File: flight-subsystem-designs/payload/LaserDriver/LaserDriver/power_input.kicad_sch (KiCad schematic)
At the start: 13 parts, among them J1 VIN Pin Header, J6 VIN Banana, J7 GND Banana, U1 LDL212PV33R, U6 UCC33420RAQR

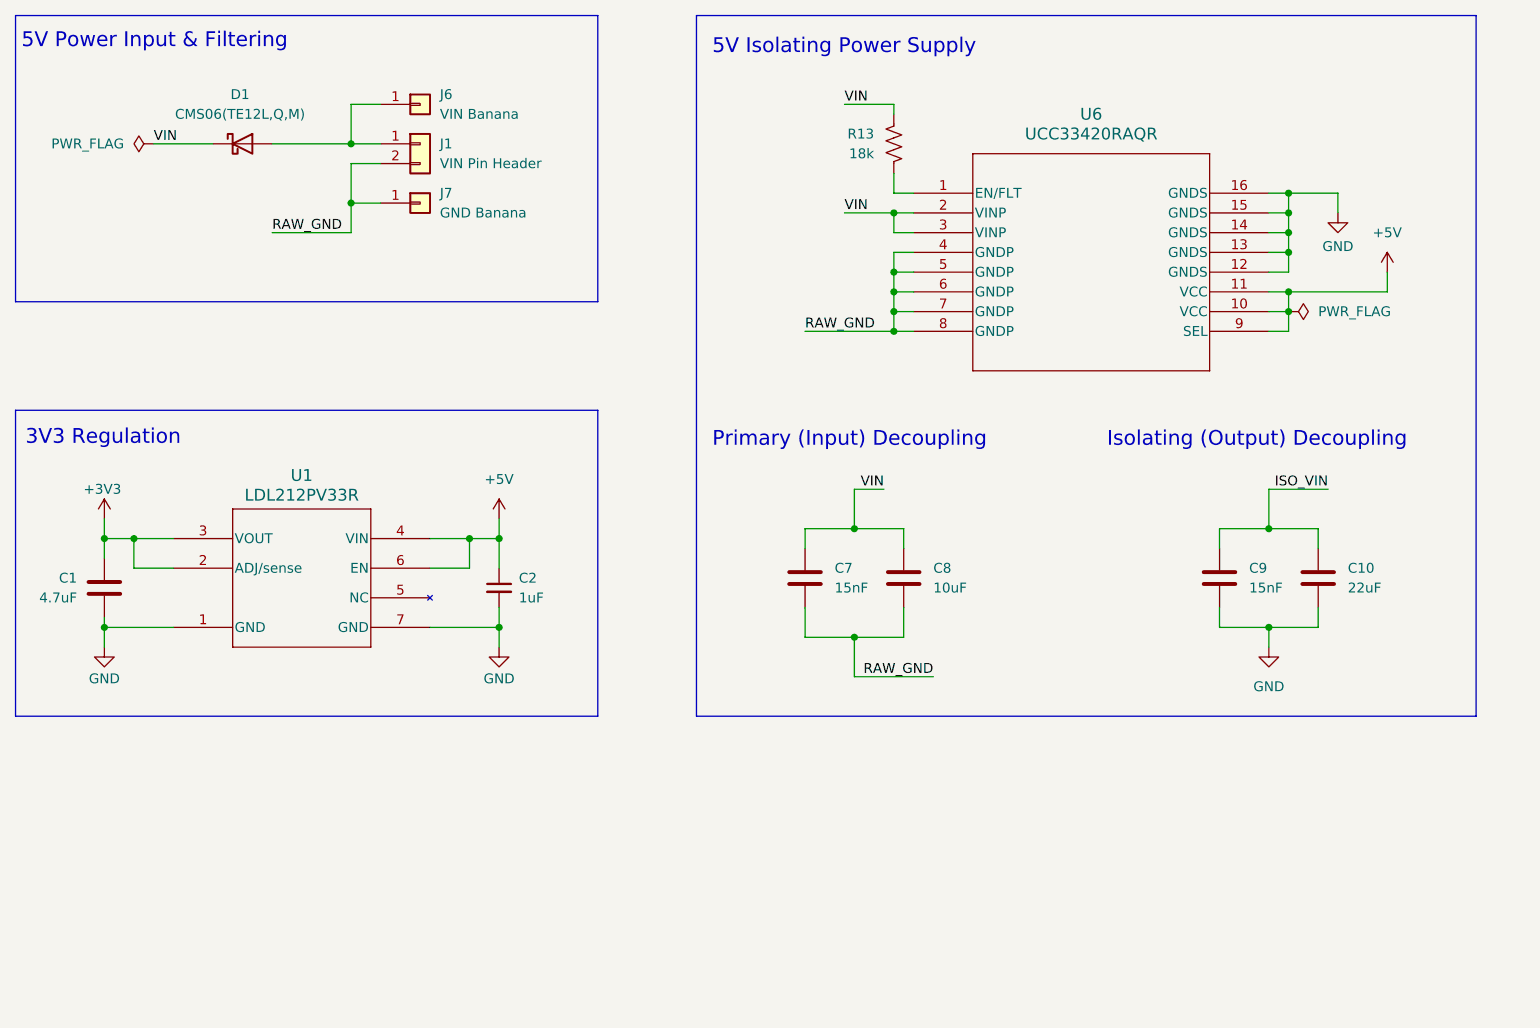
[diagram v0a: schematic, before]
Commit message: laserdriver: reset all annotations and cleared pcb :sob:
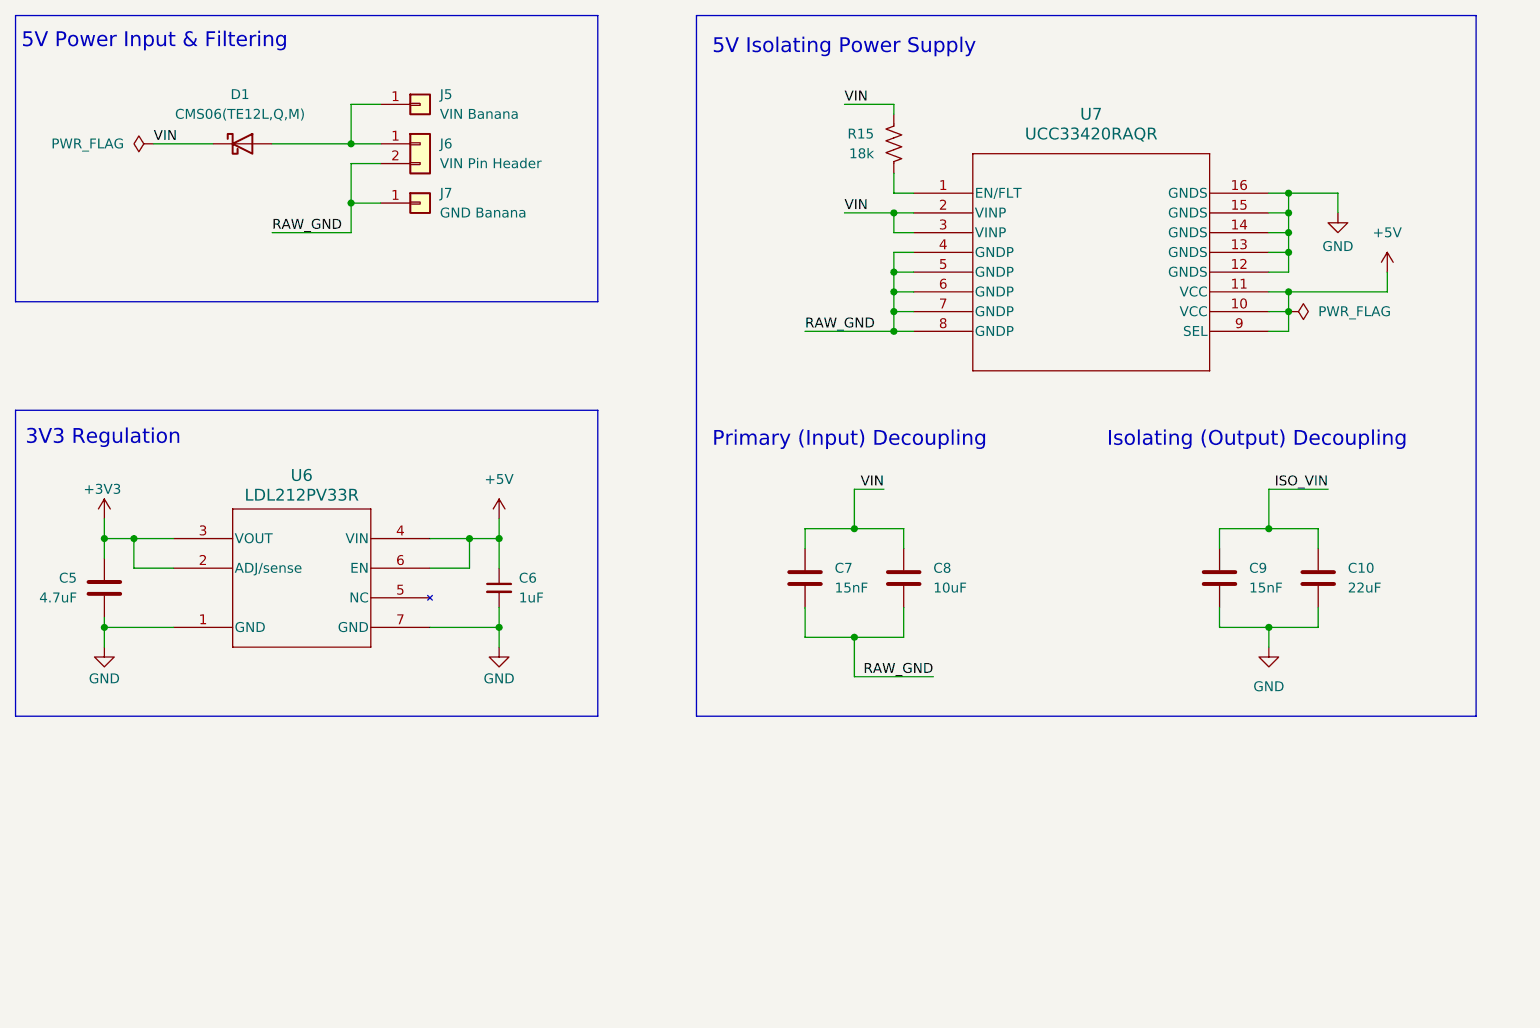
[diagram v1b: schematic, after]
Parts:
- renumbered C1 to C5, C2 to C6, J6 to J5, J1 to J6, R13 to R15, U1 to U6, U6 to U7
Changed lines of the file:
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@@
 		(on_board yes)
 		(dnp no)
-		(property "Reference" "#PWR02"
+		(property "Reference" "#PWR027"
 			(at 34.29 90.17 0)
 			(effects
@@
 			(project "LaserDriver"
 				(path "/f859ecae-83c7-438c-b2af-b7873d5255a0/55c34013-2f41-4006-a024-9ccd7006f77a"
-					(reference "#PWR02")
+					(reference "#PWR027")
 					(unit 1)
 				)
@@
 		(on_board yes)
 		(dnp no)
-		(property "Reference" "#PWR028"
+		(property "Reference" "#PWR032"
 			(at 193.04 53.34 0)
 			(effects
@@
 			(project ""
 				(path "/f859ecae-83c7-438c-b2af-b7873d5255a0/55c34013-2f41-4006-a024-9ccd7006f77a"
-					(reference "#PWR028")
+					(reference "#PWR032")
 					(unit 1)
 				)
@@
 		(dnp no)
 		(fields_autoplaced yes)
-		(property "Reference" "#PWR08"
+		(property "Reference" "#PWR031"
 			(at 184.15 109.22 0)
 			(effects
@@
 			(project ""
 				(path "/f859ecae-83c7-438c-b2af-b7873d5255a0/55c34013-2f41-4006-a024-9ccd7006f77a"
-					(reference "#PWR08")
+					(reference "#PWR031")
 					(unit 1)
 				)
@@
 		(dnp no)
 		(fields_autoplaced yes)
-		(property "Reference" "J1"
+		(property "Reference" "J6"
 			(at 77.47 38.0999 0)
 			(effects
@@
 			(project "LaserDriver"
 				(path "/f859ecae-83c7-438c-b2af-b7873d5255a0/55c34013-2f41-4006-a024-9ccd7006f77a"
-					(reference "J1")
+					(reference "J6")
 					(unit 1)
 				)
@@
 		(dnp no)
 		(fields_autoplaced yes)
-		(property "Reference" "J6"
+		(property "Reference" "J5"
 			(at 77.47 31.7499 0)
 			(effects
@@
 			(project ""
 				(path "/f859ecae-83c7-438c-b2af-b7873d5255a0/55c34013-2f41-4006-a024-9ccd7006f77a"
-					(reference "J6")
+					(reference "J5")
 					(unit 1)
 				)
@@
 		(on_board yes)
 		(dnp no)
-		(property "Reference" "C1"
+		(property "Reference" "C5"
 			(at 28.448 93.98 0)
 			(effects
@@
 			(project "LaserDriver"
 				(path "/f859ecae-83c7-438c-b2af-b7873d5255a0/55c34013-2f41-4006-a024-9ccd7006f77a"
-					(reference "C1")
+					(reference "C5")
 					(unit 1)
 				)
@@
 		(on_board yes)
 		(dnp no)
-		(property "Reference" "R13"
+		(property "Reference" "R15"
 			(at 133.35 36.8299 0)
 			(effects
@@
 			(project ""
 				(path "/f859ecae-83c7-438c-b2af-b7873d5255a0/55c34013-2f41-4006-a024-9ccd7006f77a"
-					(reference "R13")
+					(reference "R15")
 					(unit 1)
 				)
@@
 		(on_board yes)
 		(dnp no)
-		(property "Reference" "#PWR09"
+		(property "Reference" "#PWR030"
 			(at 85.09 109.22 0)
 			(effects
@@
 			(project "LaserDriver"
 				(path "/f859ecae-83c7-438c-b2af-b7873d5255a0/55c34013-2f41-4006-a024-9ccd7006f77a"
-					(reference "#PWR09")
+					(reference "#PWR030")
 					(unit 1)
 				)
@@
 		(on_board yes)
 		(dnp no)
-		(property "Reference" "#PWR03"
+		(property "Reference" "#PWR028"
 			(at 34.29 109.22 0)
 			(effects
@@
 			(project "LaserDriver"
 				(path "/f859ecae-83c7-438c-b2af-b7873d5255a0/55c34013-2f41-4006-a024-9ccd7006f77a"
-					(reference "#PWR03")
+					(reference "#PWR028")
 					(unit 1)
 				)
@@
 		(dnp no)
 		(fields_autoplaced yes)
-		(property "Reference" "#PWR033"
+		(property "Reference" "#PWR029"
 			(at 85.09 90.17 0)
 			(effects
@@
 			(project ""
 				(path "/f859ecae-83c7-438c-b2af-b7873d5255a0/55c34013-2f41-4006-a024-9ccd7006f77a"
-					(reference "#PWR033")
+					(reference "#PWR029")
 					(unit 1)
 				)
@@
 		(dnp no)
 		(fields_autoplaced yes)
-		(property "Reference" "C2"
+		(property "Reference" "C6"
 			(at 87.63 93.9862 0)
 			(effects
@@
 			(project "LaserDriver"
 				(path "/f859ecae-83c7-438c-b2af-b7873d5255a0/55c34013-2f41-4006-a024-9ccd7006f77a"
-					(reference "C2")
+					(reference "C6")
 					(unit 1)
 				)
@@
 		(dnp no)
 		(fields_autoplaced yes)
-		(property "Reference" "U6"
+		(property "Reference" "U7"
 			(at 161.29 34.29 0)
 			(effects
@@
 			(project ""
 				(path "/f859ecae-83c7-438c-b2af-b7873d5255a0/55c34013-2f41-4006-a024-9ccd7006f77a"
-					(reference "U6")
+					(reference "U7")
 					(unit 1)
 				)
@@
 		(on_board yes)
 		(dnp no)
-		(property "Reference" "U1"
+		(property "Reference" "U6"
 			(at 59.69 80.772 0)
 			(effects
@@
 			(project "LaserDriver"
 				(path "/f859ecae-83c7-438c-b2af-b7873d5255a0/55c34013-2f41-4006-a024-9ccd7006f77a"
-					(reference "U1")
+					(reference "U6")
 					(unit 1)
 				)
@@
 		(dnp no)
 		(fields_autoplaced yes)
-		(property "Reference" "#PWR029"
+		(property "Reference" "#PWR033"
 			(at 199.39 58.42 0)
 			(effects
@@
 			(project ""
 				(path "/f859ecae-83c7-438c-b2af-b7873d5255a0/55c34013-2f41-4006-a024-9ccd7006f77a"
-					(reference "#PWR029")
-					(unit 1)
-				)
+					(reference "#PWR033")
+					(unit 1)
+				)

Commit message: laserdriver: finish routing (we're so back)
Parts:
- J5, J7: footprint (none) -> Connector:Banana_Jack_1Pin
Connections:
- net ISO_VIN is gone; now on net +5V: C10.1, C9.1
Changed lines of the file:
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@@
 	(wire
 		(pts
-			(xy 184.15 87.63) (xy 184.15 82.55)
+			(xy 184.15 87.63) (xy 184.15 85.09)
 		)
 		(stroke
@@
 		(pts
 			(xy 130.81 82.55) (xy 130.81 87.63)
-		)
-		(stroke
-			(width 0)
-			(type default)
-		)
-	)
-	(wire
-		(pts
-			(xy 184.15 82.55) (xy 191.77 82.55)
 		)
 		(stroke
@@
 		)
 	)
-	(label "ISO_VIN"
-		(at 191.77 82.55 180)
-		(effects
-			(font
-				(size 1.27 1.27)
-			)
-			(justify right bottom)
-		)
-	)
 	(label "RAW_GND"
 		(at 124.46 62.23 0)
@@
 			)
 		)
-		(property "Footprint" ""
+		(property "Footprint" "Connector:Banana_Jack_1Pin"
 			(at 74.93 33.02 0)
 			(effects
@@
 			)
 		)
-		(property "Footprint" ""
+		(property "Footprint" "Connector:Banana_Jack_1Pin"
 			(at 74.93 45.72 0)
 			(effects
@@
 					(unit 1)
 				)
+			)
+		)
+	)
+	(symbol
+		(lib_id "power:+5V")
+		(at 184.15 85.09 0)
+		(unit 1)
+		(exclude_from_sim no)
+		(in_bom yes)
+		(on_board yes)
+		(dnp no)
+		(fields_autoplaced yes)
+		(property "Reference" "#PWR034"
+			(at 184.15 88.9 0)
+			(effects
+				(font
+					(size 1.27 1.27)
+				)
+				(hide yes)
+			)
+		)
+		(property "Value" "+5V"
+			(at 184.15 80.01 0)
+			(effects
+				(font
+					(size 1.27 1.27)
+				)
+			)
+		)
+		(property "Footprint" ""
+			(at 184.15 85.09 0)
+			(effects
+				(font
+					(size 1.27 1.27)
+				)
+				(hide yes)
+			)
+		)
+		(property "Datasheet" ""
+			(at 184.15 85.09 0)
+			(effects
+				(font
+					(size 1.27 1.27)
+				)
+				(hide yes)
+			)
+		)
+		(property "Description" "Power symbol creates a global label with name \"+5V\""
+			(at 184.15 85.09 0)
+			(effects
+				(font
+					(size 1.27 1.27)
+				)
+				(hide yes)
+			)
+		)
+		(pin "1"
+		)
+		(instances
+			(project ""
+				(path "/f859ecae-83c7-438c-b2af-b7873d5255a0/55c34013-2f41-4006-a024-9ccd7006f77a"
+					(reference "#PWR034")
+					(unit 1)
+				)

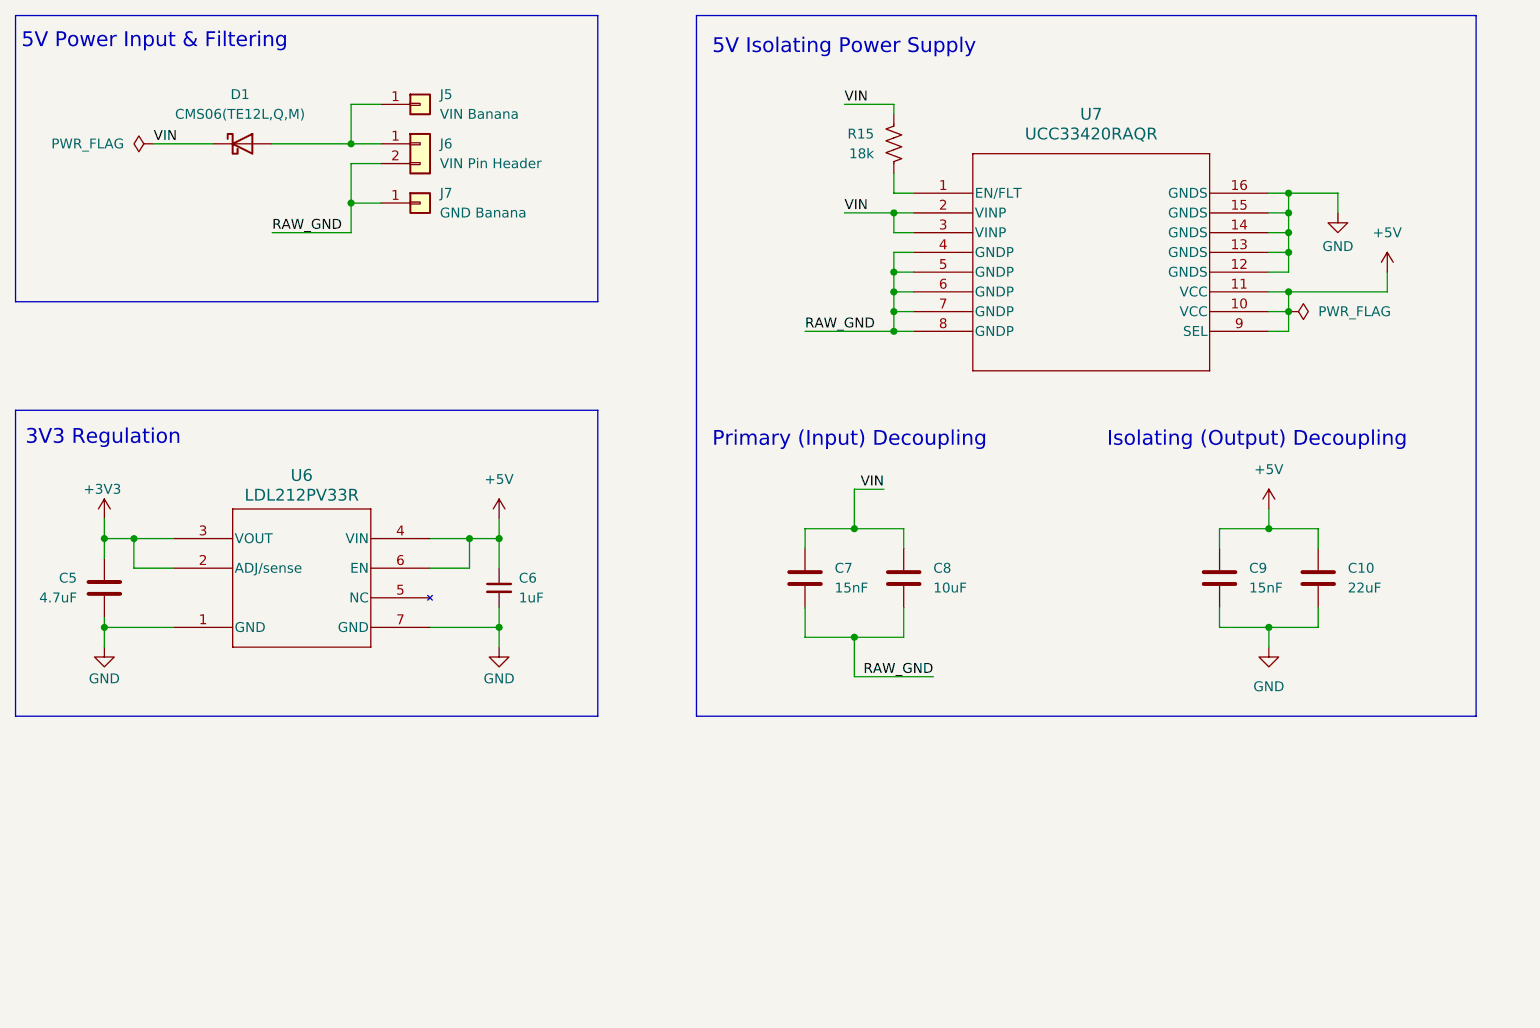
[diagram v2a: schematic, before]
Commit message: ld: v1.2.0; new LDO, corrected isopower footprint, disspation res
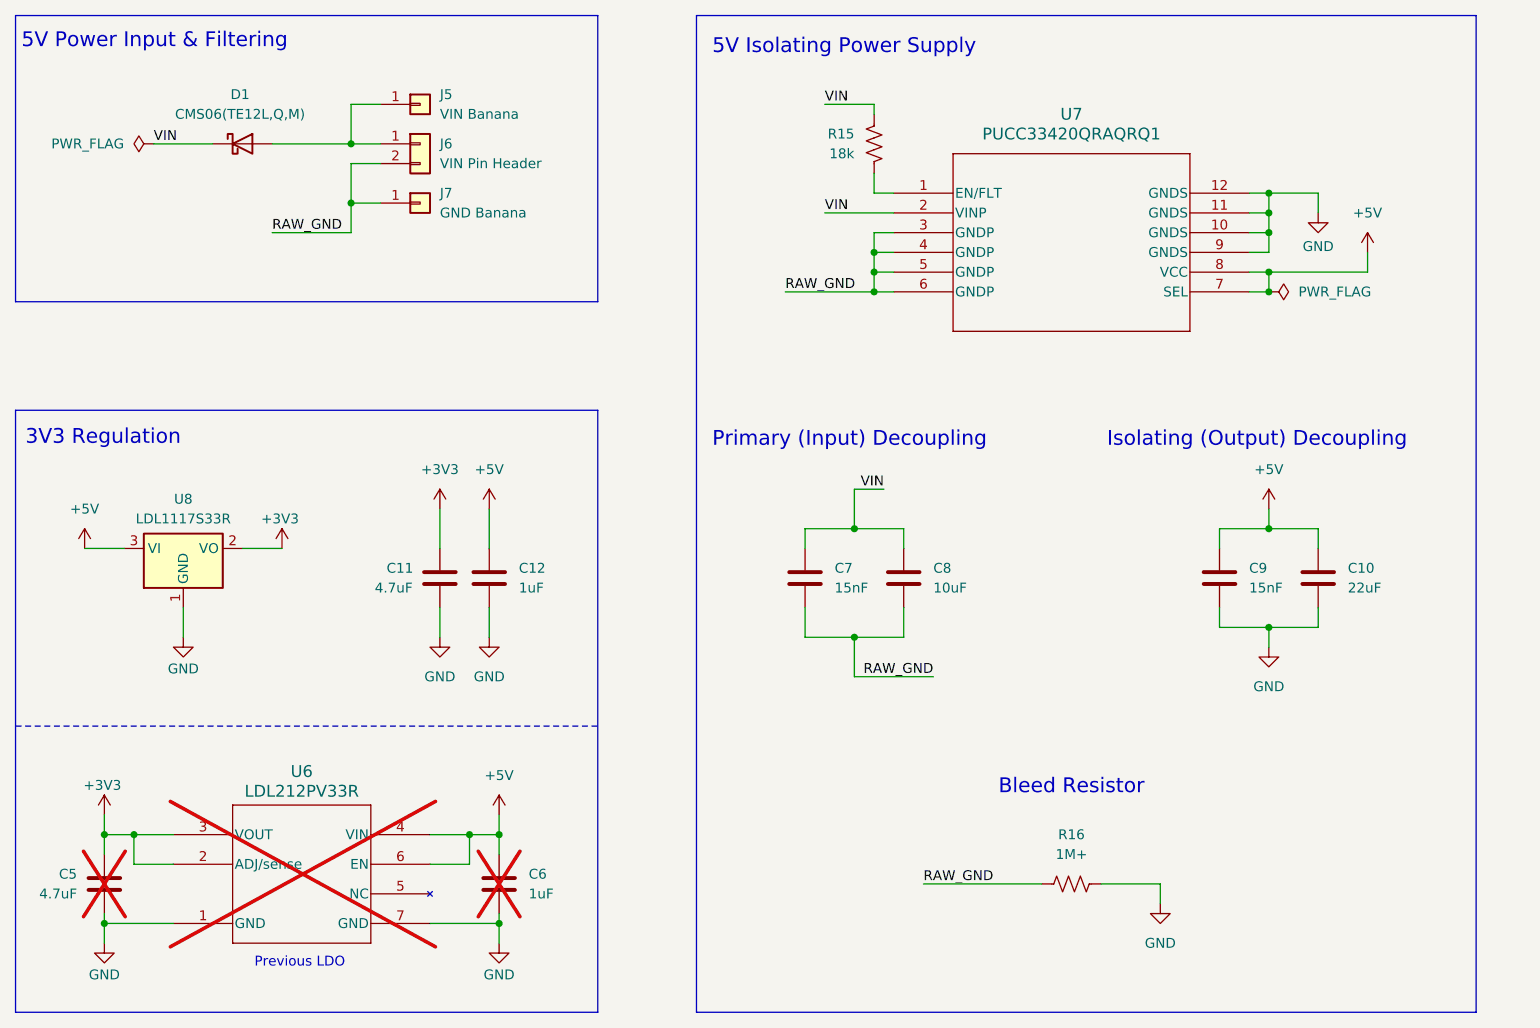
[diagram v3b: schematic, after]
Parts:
- removed C6: 1uF, Capacitor_SMD:C_0805_2012Metric_Pad1.18x1.45mm_HandSolder, symbol Device:C_Small
- removed U7: UCC33420RAQR, footprints:SSOP16_DHA_TEX, symbol UCC33421:UCC33420RAQR
- added C11: 4.7uF, Capacitor_SMD:C_0805_2012Metric_Pad1.18x1.45mm_HandSolder, symbol Device:C
- added C12, C6: 1uF, Capacitor_SMD:C_0805_2012Metric_Pad1.18x1.45mm_HandSolder, symbol Device:C
- added R16: 1M+, Resistor_SMD:R_0805_2012Metric_Pad1.20x1.40mm_HandSolder, symbol Device:R_US
- added U7: PUCC33420QRAQRQ1, footprints:VSON-FCRLF12_RAQ_TEX, symbol PUCC33420QRAQRQ1:PUCC33420QRAQRQ1
- added U8: LDL1117S33R, Package_TO_SOT_SMD:SOT-223-3_TabPin2, symbol Regulator_Linear:LD1117S33TR_SOT223
- C5: now not fitted
- U6: now not fitted; now left out of the parts list
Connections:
- net +3V3: now also C11.1, U8.2 (VO)
- net +5V: now also C12.1, C6.1, U7.7 (SEL), U7.8 (VCC), U8.3 (VI)
- net GND: now also C11.2, C12.2, C6.2, R16.2, U7.10 (GNDS), U7.11 (GNDS), U7.12 (GNDS), U7.9 (GNDS), U8.1 (GND)
- net RAW_GND: now also R16.1, U7.3 (GNDP), U7.4 (GNDP), U7.5 (GNDP), U7.6 (GNDP)
- net VIN: now also U7.2 (VINP)
- net at R15.2: now also U7.1 (EN/FLT)
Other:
- note added: "Bleed Resistor"
- note added: "Previous LDO"
